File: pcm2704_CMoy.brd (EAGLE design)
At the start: 100.3 x 77.5 mm, 70 parts, among them IC1 PCM2704, IC2 OPA2134P, IC4 7805TV, Q1 12MHz, X1 PG203J, X2 PN61729-S, X3 22-23-2031, X4 22-23-2031, X5 22-23-2031, X6 22-23-2031, X7 22-23-2021, X8 22-23-2021

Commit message: - Replaced current pot with Alps RK097
 - Removed old (virtual ground) power source

 - Added reverse polarity protection diode - still needs work (should it be a mosfet?)
 - Added polyfuse
 - Added +15V rail
 - Added -15V rail (TC962)
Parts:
- removed R12: PC16D, piher:PC16D
- removed U$1: TLE2426ILP, tle2426:TO226AA
- removed X3, X4: 22-23-2031, con-molex:22-23-2031
- removed X7, X8: 22-23-2021, con-molex:22-23-2021
- added -15V, 15V: TPTP20R, testpad:TP20R
- added C13: 22uF, rcl:E2,5-7
- added C21: 220uF, rcl:E2,5-7
- added C22, C25: 100uF, rcl:E2,5-7
- added C23, C24: 100nF, rcl:C1206
- added D1: 1N4004, diode:DO41-10
- added F1: (no value), adafruit:1812
- added FREQX2: (no value), jumper:JP1
- added IC3: 7815DT, linear:TO252
- added IC5: 7915TV, linear:TO220V
- added MP1: (no value), sym:SOT23
- added U$2: (no value), audio-pots:ALPS_RK0971221Z0X
- added U3: TC962EPA, microchip-chargepump:PDIP8_300MC
- C14, C15: value 0.1uF -> 100nF; device capacitor-wima:C7.5B4 -> rcl:C1206
- C18: value 470uF/25V -> 100uF; device rcl:E5-10,5 -> rcl:E2,5-7
- moved C15 90.5 mm to (-34.3, 71.1)
- moved C18 89.1 mm to (-10.2, 72.4)
- moved C14 79.2 mm to (-16.5, 72.4), turned to 270 degrees
- moved HID0 12.8 mm to (-6.35, -12.7)
- moved HID2 12.8 mm to (-6.35, -22.9)
- moved SJ1 12.8 mm to (-11.4, -22.9)
- moved SJ3 12.8 mm to (-11.4, -12.7)
- moved HID1 12.7 mm to (-6.35, -17.8)
- moved SJ2 12.7 mm to (-11.4, -17.8)
- moved X6 3.81 mm to (78.7, 38.1)
- renumbered IC1 to U1, IC2 to U2, R19 to RSUPP_R, R20 to RSUPP_L
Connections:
- removed net AMP_GND: C15.2, C18.-, R12.1E, R12.2E, U$1.2, U2.4, X7.2
- removed net AMP_VCC: C14.1, C18.+, U$1.3, U2.8, X7.1
- new net +15V: 15V.TP, C14.2, C18.+, IC3.2, U3.8
- new net +18V: CN1.PWR, D1.A, VCC.TP
- new net -15V: -15V.TP, C24.1, C25.-, IC5.3
- new net AMP_V+: U2.8
- new net AMP_V-: U2.4
- new net N$1: D1.C, F1.1
- new net N$24: C15.2, C21.+, F1.2, IC3.1
- new net N$30: C13.+, U3.2
- new net N$31: C13.-, U3.4
- new net N$33: FREQX2.1, U3.6
- new net N$34: C22.-, C23.1, IC5.1, U3.5
- new net S1: U$2.S1
- new net S2: U$2.S2
- net +12V: no longer CN1.PWR, VCC.TP, X8.1
- net AMP_OUT_LEFT: no longer X3.1, X4.1
- net AMP_OUT_RIGHT: no longer X3.3, X4.3
- net DAC_OUT_LEFT: now also U$2.G1; no longer R12.2A
- net DAC_OUT_RIGHT: now also U$2.G2; no longer R12.1A
- net GND: now also C14.1, C18.-, C21.-, C22.+, C23.2, C24.2, C25.+, FREQX2.2, IC3.3, IC5.2, U$2.I1, U$2.I2, U3.3; no longer C14.2, U$1.1, X3.2, X4.2, X8.2
- net N$19: now also U$2.O2; no longer R12.1S
- net N$21: now also U$2.O1; no longer R12.2S

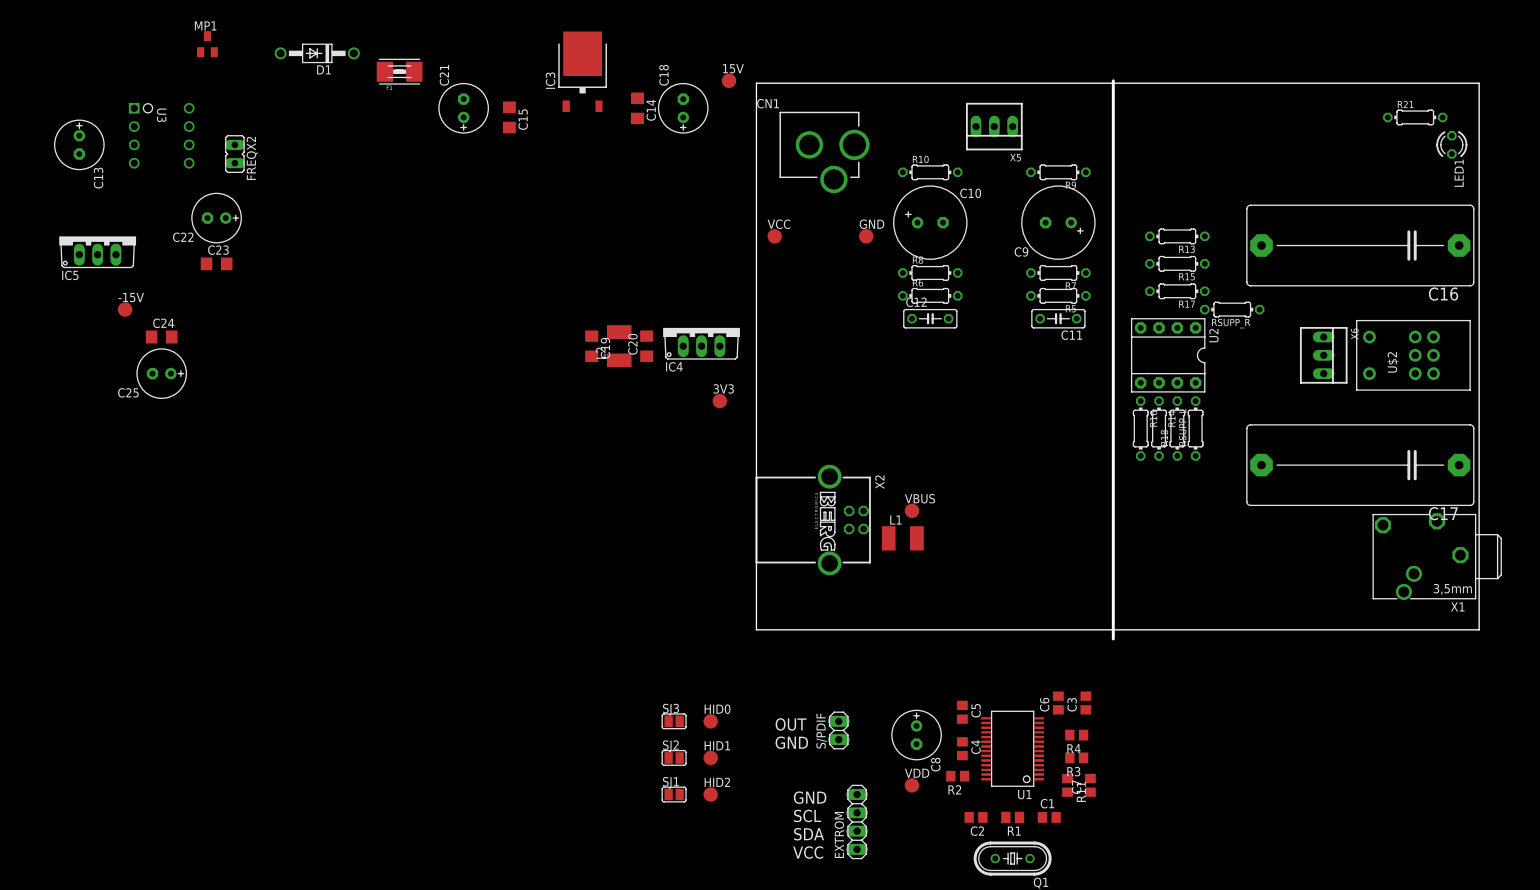
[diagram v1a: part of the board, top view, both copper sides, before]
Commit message: Minor component placement changes
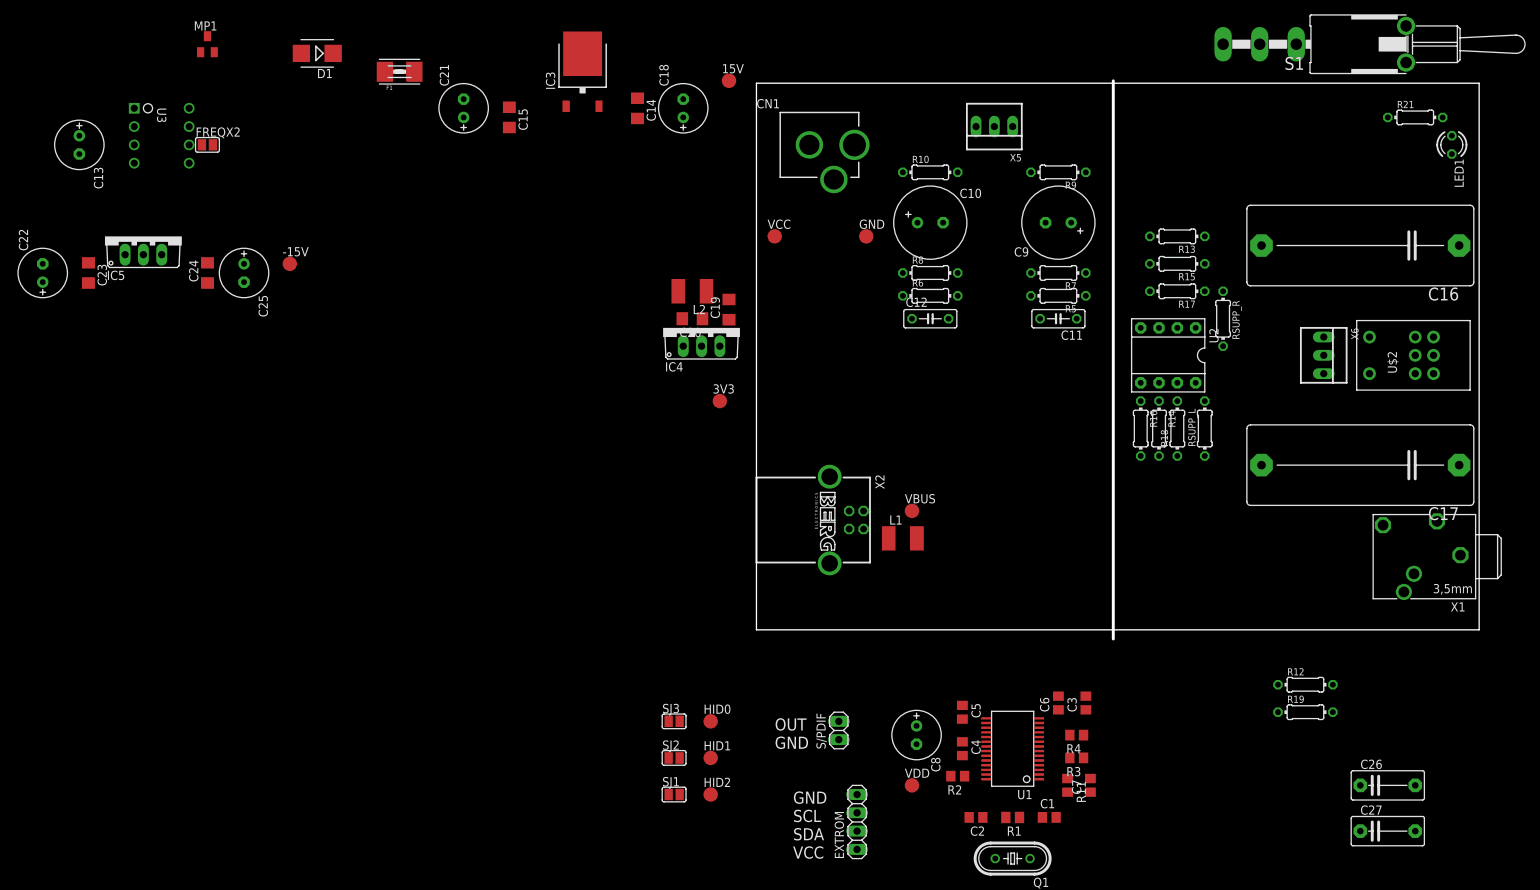
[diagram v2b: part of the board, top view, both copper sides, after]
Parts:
- added C26, C27: (no value), capacitor-wima:C7.5B4
- added R12, R19: (no value), rcl:0204/7
- added S1: (no value), switch:LPV-1
- D1: value 1N4004 -> ES2D; device diode:DO41-10 -> diode:SMB
- FREQX2: device jumper:JP1 -> jumper:SJ
- IC4: value 7805TV -> tsr 1-2433
- moved C22 25.3 mm to (-99.1, 49.5), turned to 90 degrees
- moved -15V 23.7 mm to (-64.8, 50.8)
- moved C19 19.7 mm to (-3.81, 44.5), turned to 90 degrees
- moved C25 18.1 mm to (-71.1, 49.5), turned to 270 degrees
- moved C23 17.8 mm to (-92.7, 49.5), turned to 270 degrees
- moved L2 12.7 mm to (-8.89, 47.0), turned to 180 degrees
- moved C24 10.9 mm to (-76.2, 49.5), turned to 90 degrees
- moved C20 7.41 mm to (-8.89, 43.2), turned to 180 degrees
- moved IC5 6.35 mm to (-85.1, 54.6)
- moved FREQX2 4.02 mm to (-76.2, 67.3), turned to 0 degrees
- moved RSUPP_R 1.80 mm to (64.8, 43.2), turned to 270 degrees
- moved RSUPP_L 1.27 mm to (62.2, 27.9)
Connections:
- removed net AMP_V+: U2.8
- removed net AMP_V-: U2.4
- new net N$33: RSUPP_R.2, U2.1
- new net N$35: RSUPP_L.2, U2.7
- new net N$36: C26.1, R12.2
- new net N$37: C26.2, R12.1
- net +15V: now also U2.8
- net -15V: now also U2.4
- net AMP_OUT_LEFT: now also R17.1
- net AMP_OUT_RIGHT: now also R18.1
- net N$13: now also C27.2, R19.1; no longer R17.1, RSUPP_R.2, U2.1
- net N$14: now also C27.1, R19.2; no longer R18.1, RSUPP_L.2, U2.7

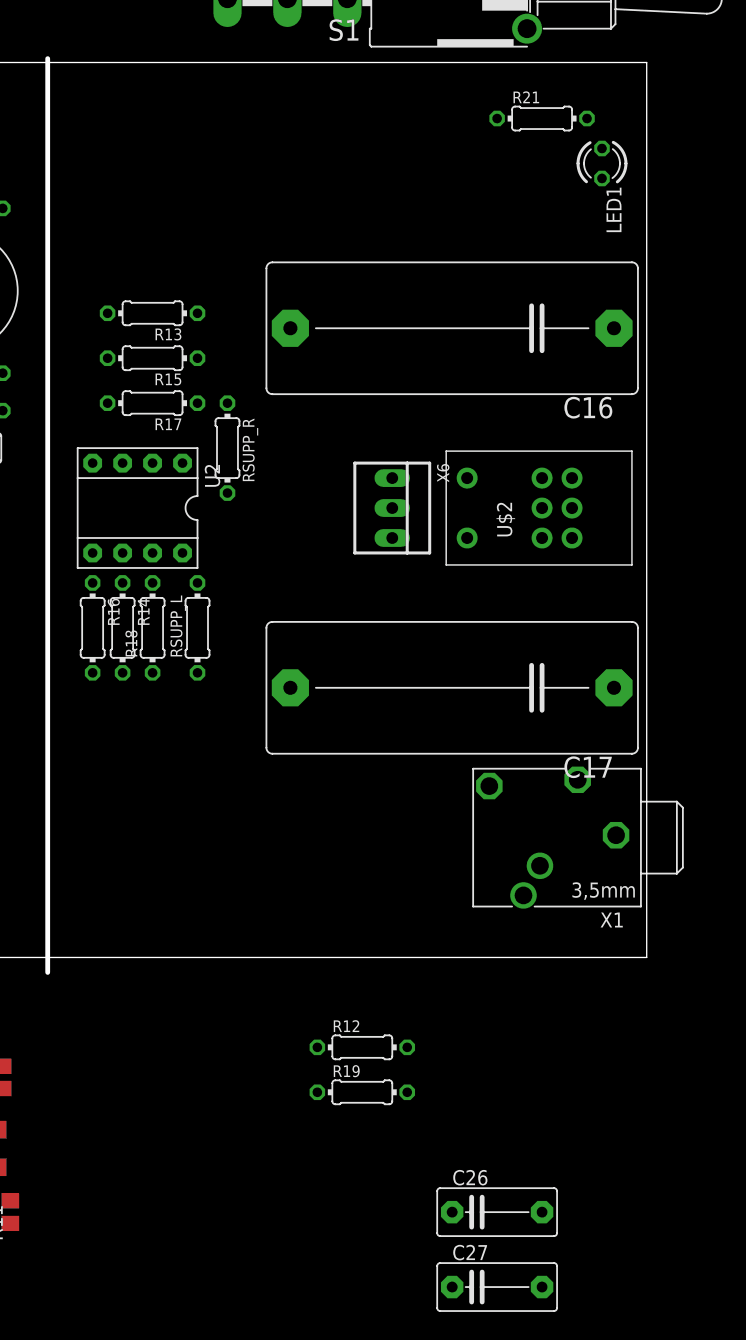
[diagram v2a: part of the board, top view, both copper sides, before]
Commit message: - Replaced the audio jack with a PF325
 - Renamed the resistors and the capacitors in the amp to reflect the side they are used on (R/L)
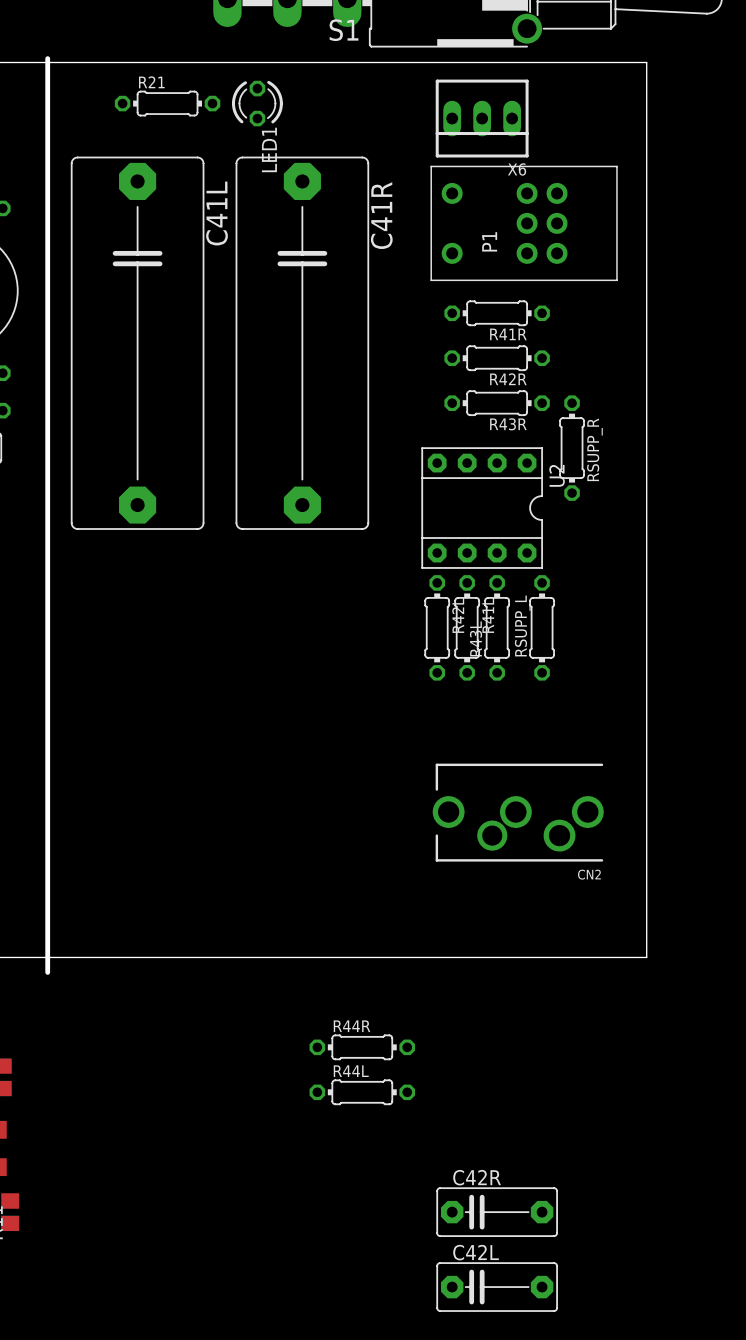
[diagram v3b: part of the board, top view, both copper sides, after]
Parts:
- removed C16, C17: 0.47uF, capacitor-wima:C27.5B11
- removed R13, R14: 100K, rcl:0204/7
- removed R15, R16: 2.2K, rcl:0204/7
- removed R17, R18: 10K, rcl:0204/7
- removed U$2: (no value), audio-pots:ALPS_RK0971221Z0X
- removed X1: PG203J, con-hirschmann:PG203J
- added C41L, C41R: 0.47uF, capacitor-wima:C27.5B11
- added CN2: (no value), microbuilder:4UCONN_05550
- added P1: (no value), audio-pots:ALPS_RK0971221Z0X
- added R41L, R41R: 100K, rcl:0204/7
- added R42L, R42R: 2.2K, rcl:0204/7
- added R43L, R43R: 10K, rcl:0204/7
- moved X6 33.9 mm to (86.4, 71.1), turned to 180 degrees
- moved R21 31.8 mm to (59.7, 72.4)
- moved LED1 29.6 mm to (67.3, 72.4)
- moved RSUPP_R 29.2 mm to (94.0, 43.2)
- moved RSUPP_L 29.2 mm to (91.4, 27.9)
- moved U2 29.2 mm to (86.4, 38.1)
- renumbered C26 to C42R, C27 to C42L, R12 to R44R, R19 to R44L
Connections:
- net AMP_OUT_LEFT: now also CN2.5, R43R.1; no longer R17.1, X1.5
- net AMP_OUT_RIGHT: now also CN2.3, R43L.1; no longer R18.1, X1.2
- net DAC_OUT_LEFT: now also P1.G1; no longer U$2.G1
- net DAC_OUT_RIGHT: now also P1.G2; no longer U$2.G2
- net GND: now also CN2.1, P1.I1, P1.I2, R41L.2, R41R.1, R42L.2, R42R.1; no longer R13.1, R14.2, R15.1, R16.2, U$2.I1, U$2.I2, X1.1
- net N$17: now also C41L.2, R41L.1; no longer C17.2, R14.1
- net N$18: now also C41R.2, R41R.2; no longer C16.2, R13.2
- net N$19: now also C41R.1, P1.O2; no longer C16.1, U$2.O2
- net N$21: now also C41L.1, P1.O1; no longer C17.1, U$2.O1
- net N$22: now also R42R.2, R43R.2; no longer R15.2, R17.2
- net N$23: now also R42L.1, R43L.2; no longer R16.1, R18.2
- net S1: now also P1.S1; no longer U$2.S1
- net S2: now also P1.S2; no longer U$2.S2

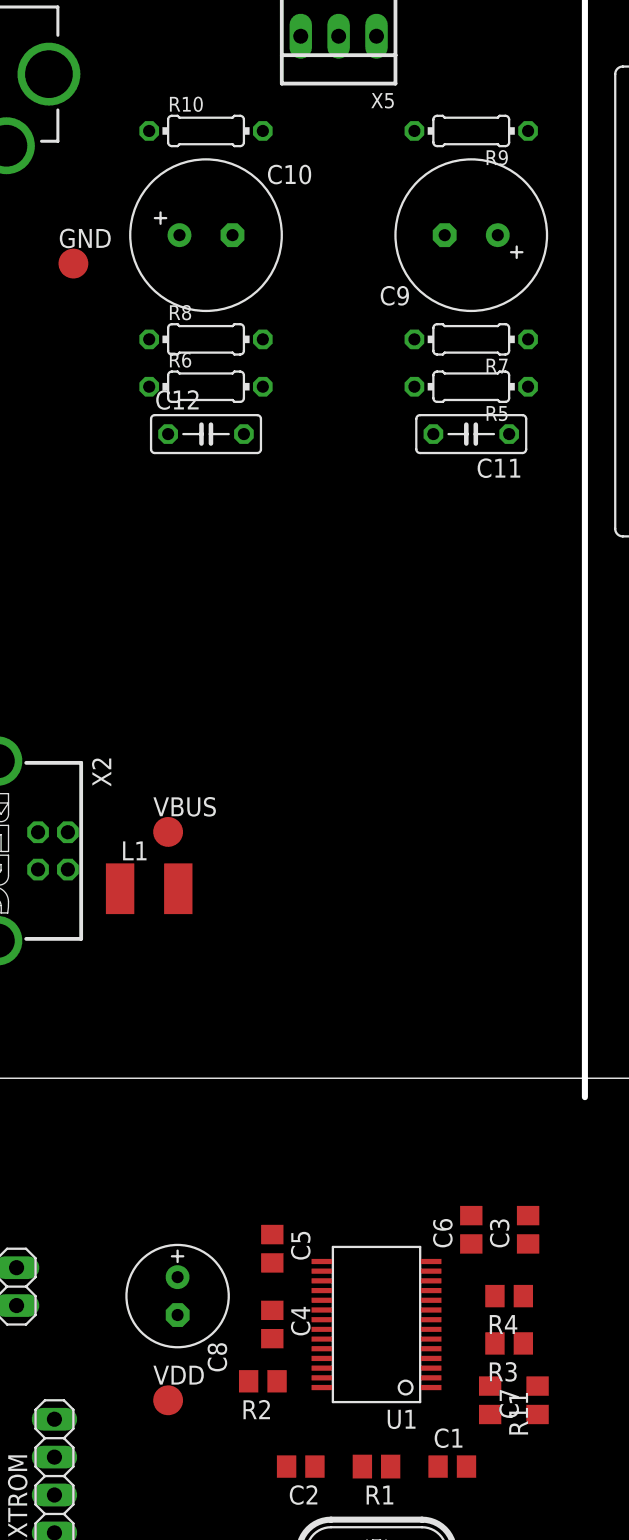
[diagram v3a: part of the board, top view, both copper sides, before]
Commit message: - Modified PCM2704 to be self powered
 - Modified the resistor names of the dac to match the example schematic in the datasheet
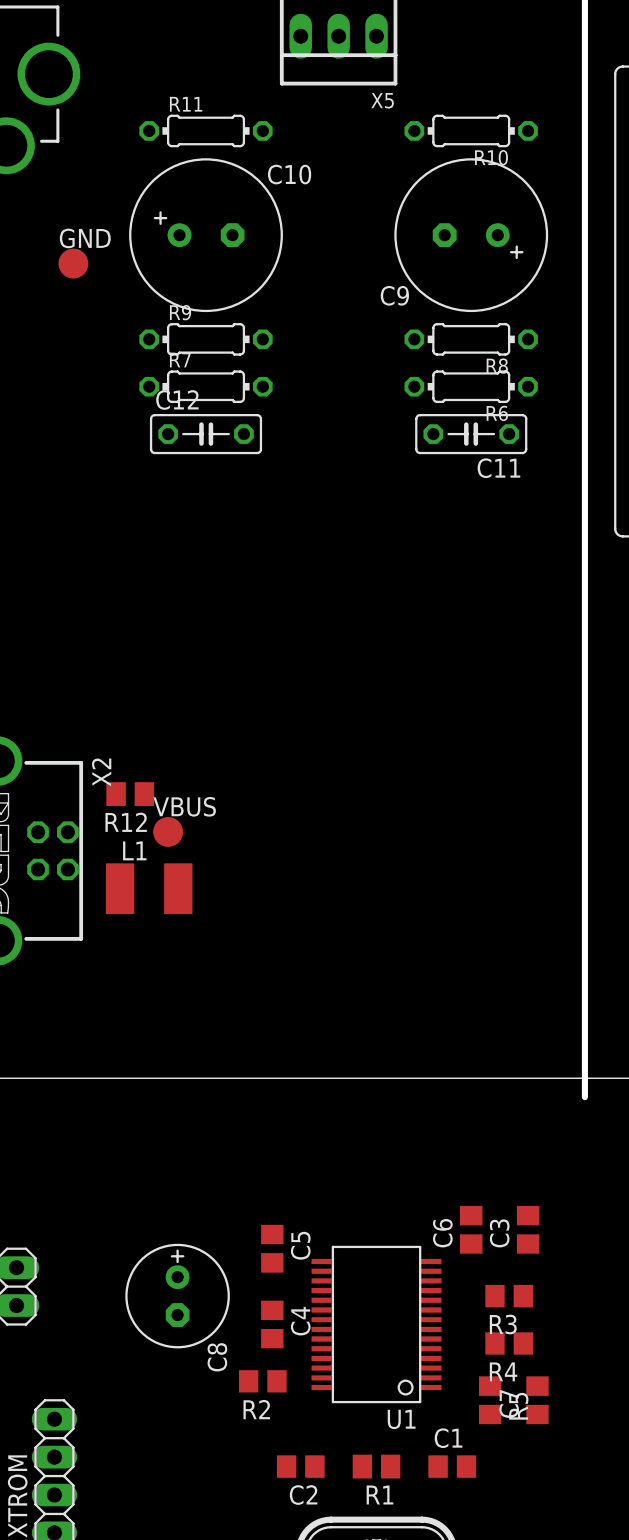
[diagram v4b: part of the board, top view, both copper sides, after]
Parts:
- removed VDD: TPTP20R, testpad:TP20R
- added R12: 1M, rcl:M0805
- R11: value 1k5 -> 3k3; device rcl:R0805 -> rcl:0204/7
- R5: value 16R -> 1k5; device rcl:0204/7 -> rcl:R0805
- R7: value 3k3 -> 16R
- moved R11 87.2 mm to (24.1, 63.5), turned to 0 degrees
- moved R5 68.0 mm to (43.2, -21.6), turned to 270 degrees
- moved R9 22.6 mm to (24.1, 49.5), turned to 0 degrees
- moved R7 18.1 mm to (24.1, 46.4), turned to 0 degrees
- moved R10 17.8 mm to (41.9, 63.5), turned to 180 degrees
- moved R6 17.8 mm to (41.9, 46.4), turned to 180 degrees
- moved R8 17.8 mm to (41.9, 49.5), turned to 180 degrees
- moved R3 3.18 mm to (44.5, -14.6)
- moved R4 3.18 mm to (44.5, -17.8)
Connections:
- removed net VCCL: C6.2, U1.13
- removed net VCCP: C4.1, EXTROM.1, U1.20
- removed net VCCR: C5.1, U1.16
- removed net VDD: C7.2, R11.1, R2.2, U1.25, U1.26, U1.4, U1.7, VDD.TP
- net +3V3: now also C4.2, C5.1, C6.2, C7.2, EXTROM.1, R5.1, U1.10, U1.13, U1.16, U1.20, U1.25, U1.26, U1.7
- net DAC_OUT_LEFT: now also R11.2; no longer R10.2
- net DAC_OUT_RIGHT: now also R10.2; no longer R9.2
- net GND: now also C4.1, R11.1, U1.4; no longer C3.2, C4.2, R5.1, U1.21
- net N$2: now also R12.2; no longer L1.1
- net N$20: now also R5.2; no longer R11.2
- net N$26: now also R6.2; no longer R5.2
- net N$27: now also R7.2; no longer R6.2
- net N$28: now also R8.2; no longer R7.2
- net N$29: now also R9.2; no longer R8.2
- net N$3: now also R4.1; no longer R3.1
- net N$4: now also R4.2; no longer R3.2
- net N$5: now also R3.1; no longer R4.1
- net N$6: now also R3.2; no longer R4.2
- net VBUS: now also R12.1, U1.21; no longer C3.1, L1.2, U1.10
